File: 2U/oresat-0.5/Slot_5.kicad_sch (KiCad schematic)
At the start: 3 parts, among them J1 m55-6001642

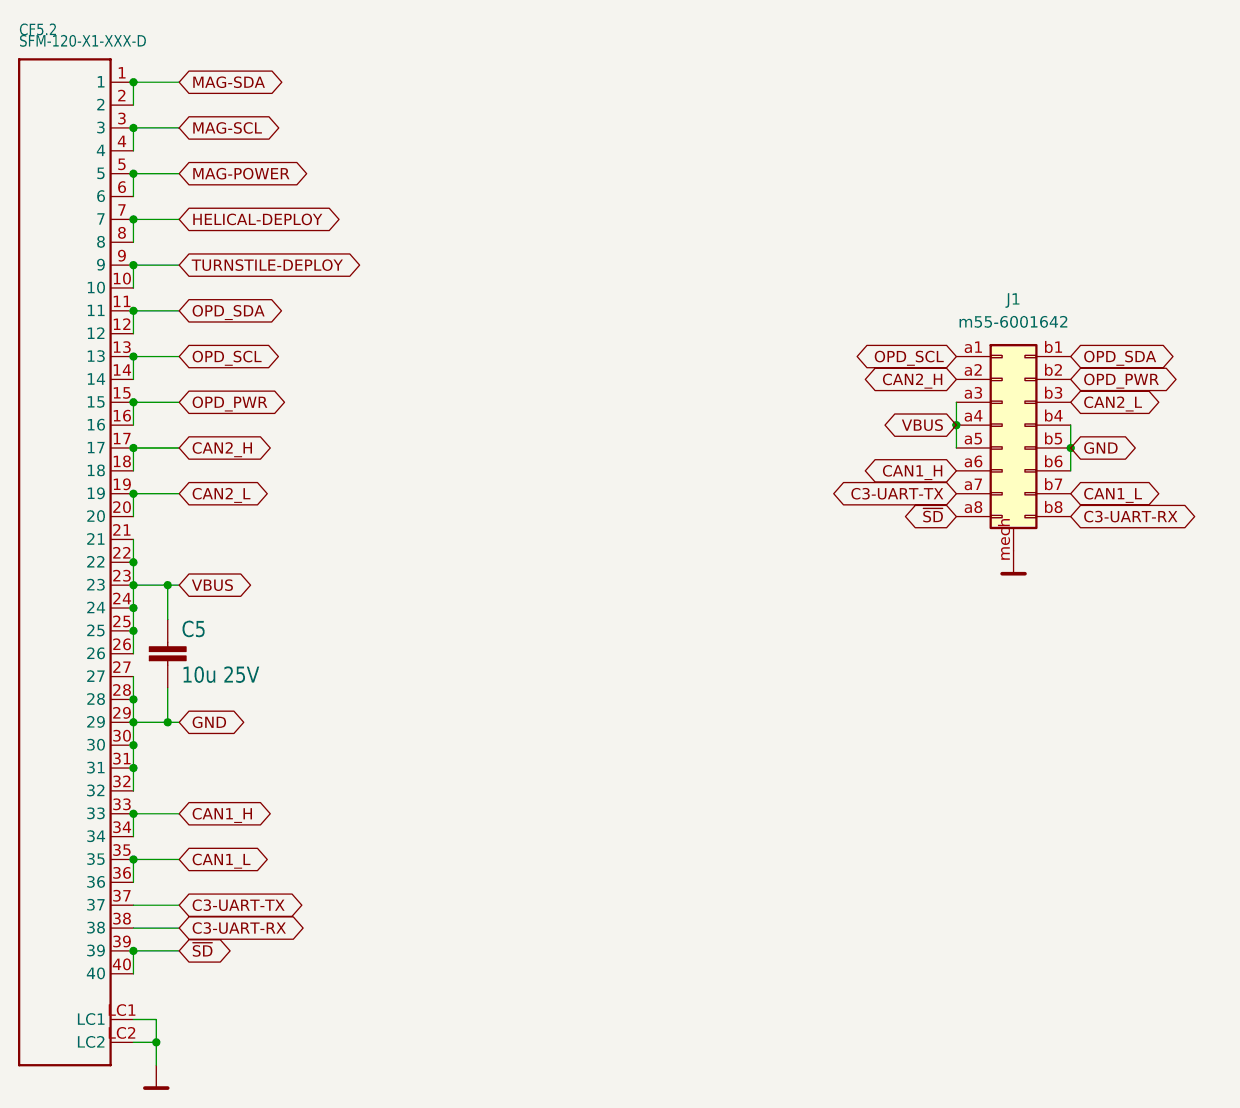
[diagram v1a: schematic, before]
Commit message: Fixed all (most) of the issues from Eagle imports
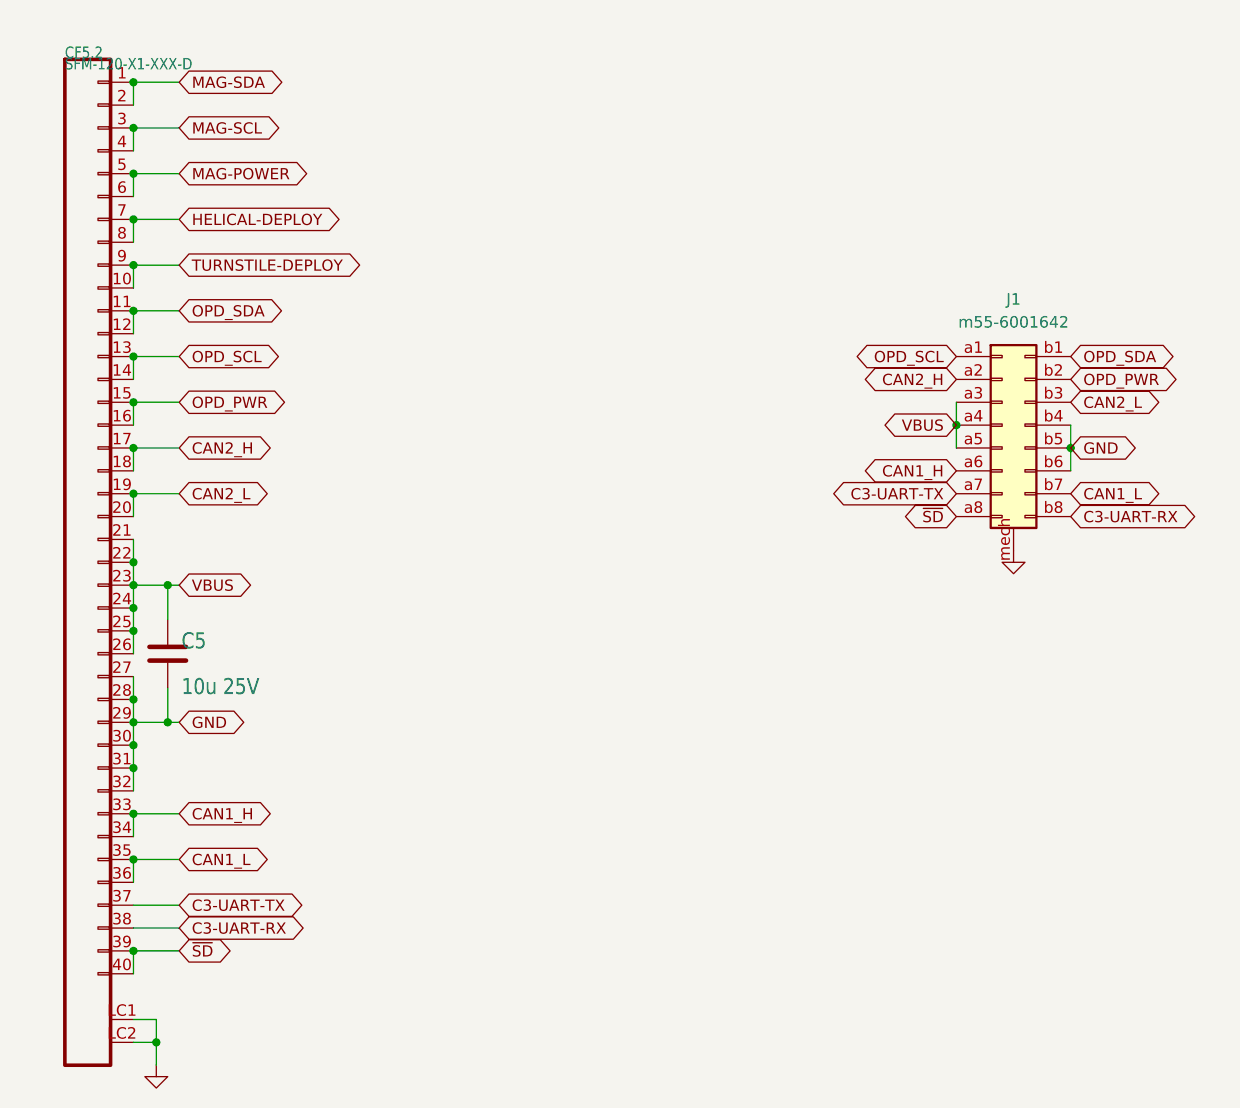
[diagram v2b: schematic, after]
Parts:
- C5: symbol oresat0-1u-backplane-eagle-import:C-EU1206-B -> Device:C
- CF5.2: symbol oresat-backplane-2u-eagle-import:SFM-120-X1-XXX-D -> oresat-connectors:J-SAMTEC-TFM-120-01-L-D-RA

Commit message: Moved entire schematic to single page
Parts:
- removed C5: 10u 25V, Capacitor_SMD:C_1206_3216Metric, symbol Device:C
- removed CF5.2: SFM-120-X1-XXX-D, oresat-connectors:J-SAMTEC-SFM-120-X1-XXX-D, symbol oresat-connectors:J-SAMTEC-TFM-120-01-L-D-RA
- removed J1: m55-6001642, oresat-connectors:m55-6001642, symbol oresat-connectors:m55-6001642
